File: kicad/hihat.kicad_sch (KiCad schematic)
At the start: 51 parts, among them J1 Synth_power_2x5, J10 brain_south, J11 CVin, J2 CH trig, J3 accent, J5 ctrl_north, J6 brain_north, J7 OH trig, J9 ctrl_south, SW1 mute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

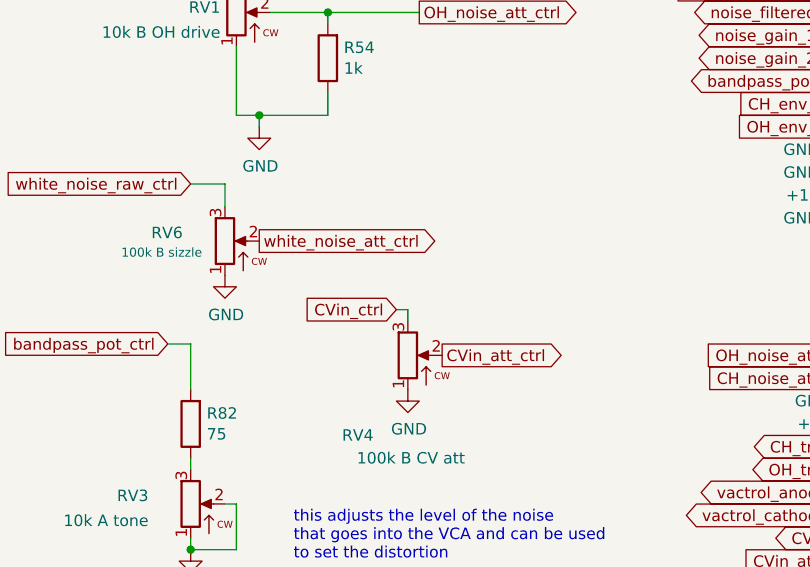
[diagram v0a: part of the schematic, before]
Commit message: fix noise section (1uF instead of 10uF), location of switch jacks!!, add resistor to make sizzle pot log-like and add note to use socket for cap to adjust tight decay
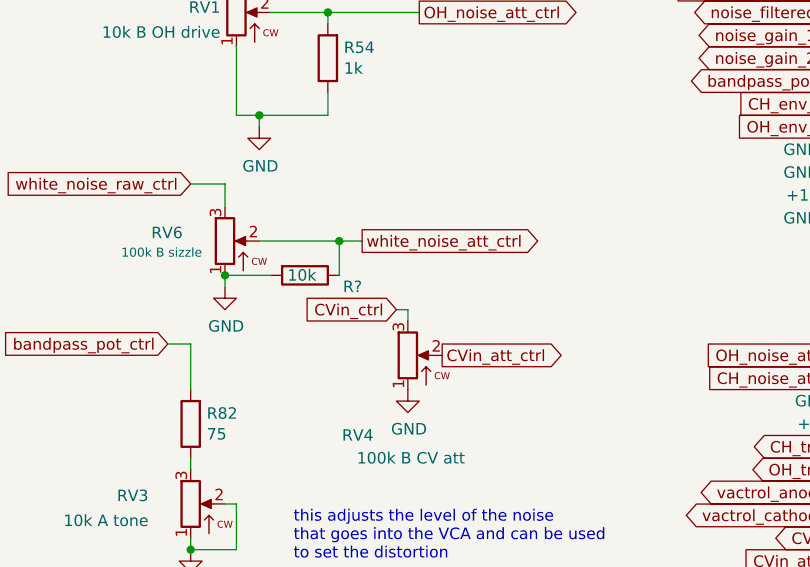
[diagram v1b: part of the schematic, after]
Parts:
- added R?: 10k, ao_tht:R_Axial_DIN0207_L6.3mm_D2.5mm_P10.16mm_Horizontal, symbol ao_symbols:R
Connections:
- net GND: now also R?.2
- net white_noise_att_ctrl: now also R?.1
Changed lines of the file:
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@@
   (junction (at 52.07 181.61) (diameter 0) (color 0 0 0 0)
   )
+  (junction (at 40.64 120.65) (diameter 0) (color 0 0 0 0)
+  )
   (junction (at 220.726 148.59) (diameter 0) (color 0 0 0 0)
   )
@@
   (junction (at 129.54 189.23) (diameter 0) (color 0 0 0 0)
   )
+  (junction (at 53.34 116.84) (diameter 0) (color 0 0 0 0)
+  )
   (junction (at 57.15 41.91) (diameter 0) (color 0 0 0 0)
   )
@@
     (stroke (width 0) (type default) (color 0 0 0 0))
   )
+  (wire (pts (xy 53.34 116.84) (xy 55.88 116.84))
+    (stroke (width 0) (type default) (color 0 0 0 0))
+  )
+  (wire (pts (xy 40.64 120.65) (xy 45.72 120.65))
+    (stroke (width 0) (type default) (color 0 0 0 0))
+  )
   (wire (pts (xy 187.706 133.35) (xy 199.136 133.35))
     (stroke (width 0) (type default) (color 0 0 0 0))
@@
     (stroke (width 0) (type default) (color 0 0 0 0))
   )
+  (wire (pts (xy 40.64 120.65) (xy 40.64 121.92))
+    (stroke (width 0) (type default) (color 0 0 0 0))
+  )
   (wire (pts (xy 41.91 73.66) (xy 41.91 66.04))
     (stroke (width 0) (type default) (color 0 0 0 0))
@@
     (stroke (width 0) (type default) (color 0 0 0 0))
   )
+  (wire (pts (xy 53.34 120.65) (xy 53.34 116.84))
+    (stroke (width 0) (type default) (color 0 0 0 0))
+  )
   (wire (pts (xy 271.526 76.2) (xy 272.796 76.2))
     (stroke (width 0) (type default) (color 0 0 0 0))
@@
     (stroke (width 0) (type default) (color 0 0 0 0))
   )
+  (wire (pts (xy 44.45 116.84) (xy 53.34 116.84))
+    (stroke (width 0) (type default) (color 0 0 0 0))
+  )
   (wire (pts (xy 153.67 190.5) (xy 153.67 184.15))
     (stroke (width 0) (type default) (color 0 0 0 0))
@@
     )
   )
-  (global_label "white_noise_att_ctrl" (shape output) (at 44.45 116.84 0) (fields_autoplaced)
+  (global_label "white_noise_att_ctrl" (shape output) (at 55.88 116.84 0) (fields_autoplaced)
     (effects (font (size 1.27 1.27)) (justify left))
-    (property "Intersheet References" "${INTERSHEET_REFS}" (id 0) (at 65.4613 116.7606 0)
+    (property "Intersheet References" "${INTERSHEET_REFS}" (id 0) (at 76.8913 116.7606 0)
       (effects (font (size 1.27 1.27)) (justify left) hide)
     )
@@
     (pin "3")
   )
+  (symbol (lib_id "ao_symbols:R") (at 49.53 120.65 270) (unit 1)
+    (in_bom yes) (on_board yes)
+    (property "Reference" "R?" (id 0) (at 55.88 121.92 90)
+      (effects (font (size 1.27 1.27)) (justify right))
+    )
+    (property "Value" "10k" (id 1) (at 50.8 120.65 90)
+      (effects (font (size 1.27 1.27)) (justify right))
+    )
+    (property "Footprint" "ao_tht:R_Axial_DIN0207_L6.3mm_D2.5mm_P10.16mm_Horizontal" (id 2) (at 49.53 118.872 90)
+      (effects (font (size 1.27 1.27)) hide)
+    )
+    (property "Datasheet" "" (id 3) (at 49.53 120.65 0)
+      (effects (font (size 1.27 1.27)) hide)
+    )
+    (property "Vendor" "Tayda" (id 4) (at 49.53 120.65 0)
+      (effects (font (size 1.27 1.27)) hide)
+    )
+    (pin "1")
+    (pin "2")
+  )
   (symbol (lib_id "ao_symbols:R") (at 205.486 97.79 180) (unit 1)
     (in_bom yes) (on_board yes)
@@
     (pin "2")
   )
-  (symbol (lib_id "power:GND") (at 40.64 120.65 0) (unit 1)
+  (symbol (lib_id "power:GND") (at 40.64 121.92 0) (unit 1)
     (in_bom yes) (on_board yes)
-    (property "Reference" "#PWR0201" (id 0) (at 40.64 127 0)
+    (property "Reference" "#PWR0201" (id 0) (at 40.64 128.27 0)
       (effects (font (size 1.27 1.27)) hide)
     )
-    (property "Value" "GND" (id 1) (at 40.767 125.0442 0))
-    (property "Footprint" "" (id 2) (at 40.64 120.65 0)
+    (property "Value" "GND" (id 1) (at 40.767 126.3142 0))
+    (property "Footprint" "" (id 2) (at 40.64 121.92 0)
       (effects (font (size 1.27 1.27)) hide)
     )
-    (property "Datasheet" "" (id 3) (at 40.64 120.65 0)
+    (property "Datasheet" "" (id 3) (at 40.64 121.92 0)
       (effects (font (size 1.27 1.27)) hide)
     )
@@
     )
     (path "/b5be6f70-cd5c-44bc-97f4-a37a69269913/5574f28f-2f42-4307-a989-4d5c5cb72409"
-      (reference "C26") (unit 1) (value "10u") (footprint "ao_tht:CP_Radial_horizontalflat_D5mm_P2.50mm_H10mm")
+      (reference "C26") (unit 1) (value "1u") (footprint "ao_tht:CP_Radial_horizontalflat_D5mm_P2.50mm_H10mm")
     )
     (path "/eacdee85-b62a-4dac-9379-30bbbe70428b/98e42427-bc70-486b-b6fe-74d9041e3d76"
@@
       (reference "R82") (unit 1) (value "75") (footprint "ao_tht:R_Axial_DIN0207_L6.3mm_D2.5mm_P10.16mm_Horizontal")
     )
+    (path "/4cddb568-0771-4bda-b25c-c9ebb5c9c2f2"
+      (reference "R?") (unit 1) (value "10k") (footprint "ao_tht:R_Axial_DIN0207_L6.3mm_D2.5mm_P10.16mm_Horizontal")
+    )
     (path "/9c615a4f-0121-4c09-a99f-26fb1769292a"

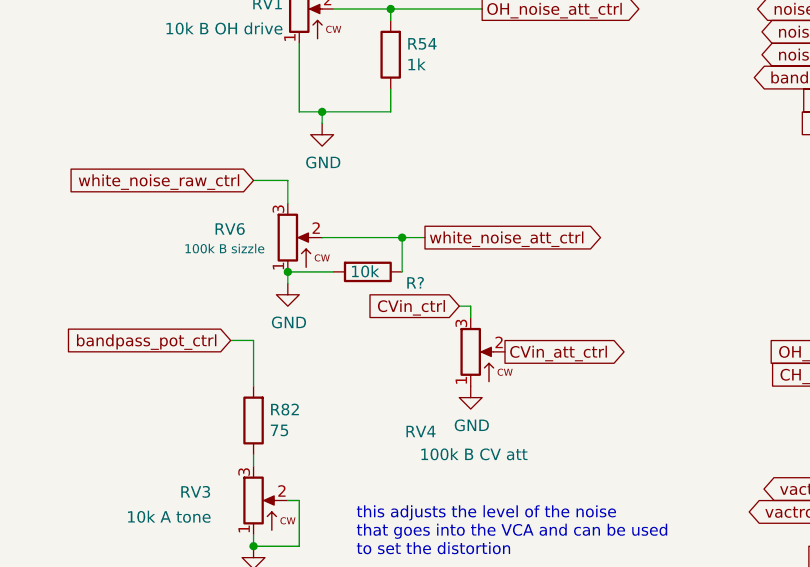
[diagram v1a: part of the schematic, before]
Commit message: add resistor reference
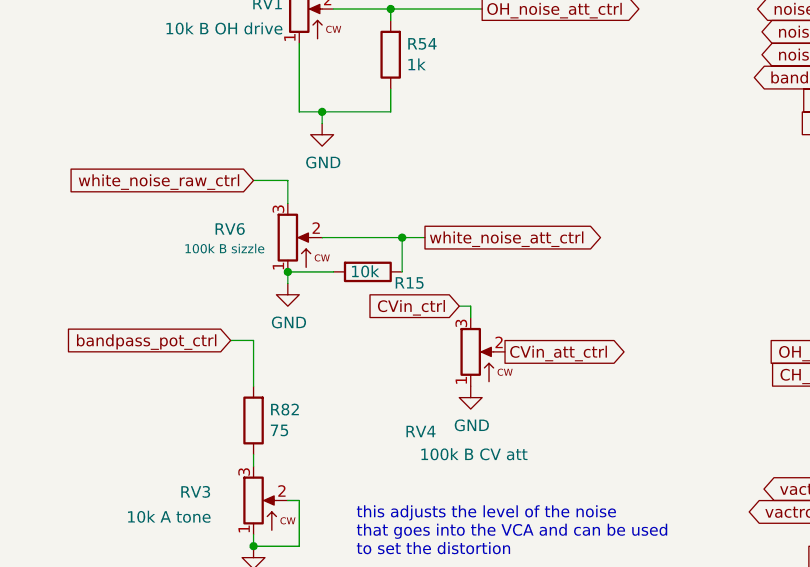
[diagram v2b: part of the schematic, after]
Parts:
- gave numbers to parts that had none: 1
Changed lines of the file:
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@@
   (symbol (lib_id "ao_symbols:R") (at 49.53 120.65 270) (unit 1)
     (in_bom yes) (on_board yes)
-    (property "Reference" "R?" (id 0) (at 55.88 121.92 90)
+    (property "Reference" "R15" (id 0) (at 55.88 121.92 90)
       (effects (font (size 1.27 1.27)) (justify right))
     )
@@
       (reference "R14") (unit 1) (value "18k") (footprint "ao_tht:R_Axial_DIN0207_L6.3mm_D2.5mm_P10.16mm_Horizontal")
     )
+    (path "/4cddb568-0771-4bda-b25c-c9ebb5c9c2f2"
+      (reference "R15") (unit 1) (value "10k") (footprint "ao_tht:R_Axial_DIN0207_L6.3mm_D2.5mm_P10.16mm_Horizontal")
+    )
     (path "/b5be6f70-cd5c-44bc-97f4-a37a69269913/e10935e8-de7f-444a-b9ba-c26c46877310"
       (reference "R16") (unit 1) (value "100k") (footprint "ao_tht:R_Axial_DIN0207_L6.3mm_D2.5mm_P10.16mm_Horizontal")
@@
       (reference "R82") (unit 1) (value "75") (footprint "ao_tht:R_Axial_DIN0207_L6.3mm_D2.5mm_P10.16mm_Horizontal")
     )
-    (path "/4cddb568-0771-4bda-b25c-c9ebb5c9c2f2"
-      (reference "R?") (unit 1) (value "10k") (footprint "ao_tht:R_Axial_DIN0207_L6.3mm_D2.5mm_P10.16mm_Horizontal")
-    )
     (path "/9c615a4f-0121-4c09-a99f-26fb1769292a"
